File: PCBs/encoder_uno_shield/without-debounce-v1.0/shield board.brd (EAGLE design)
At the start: 71.7 x 53.5 mm, 9 parts, among them U1 ARDUINOR3-BPLACE

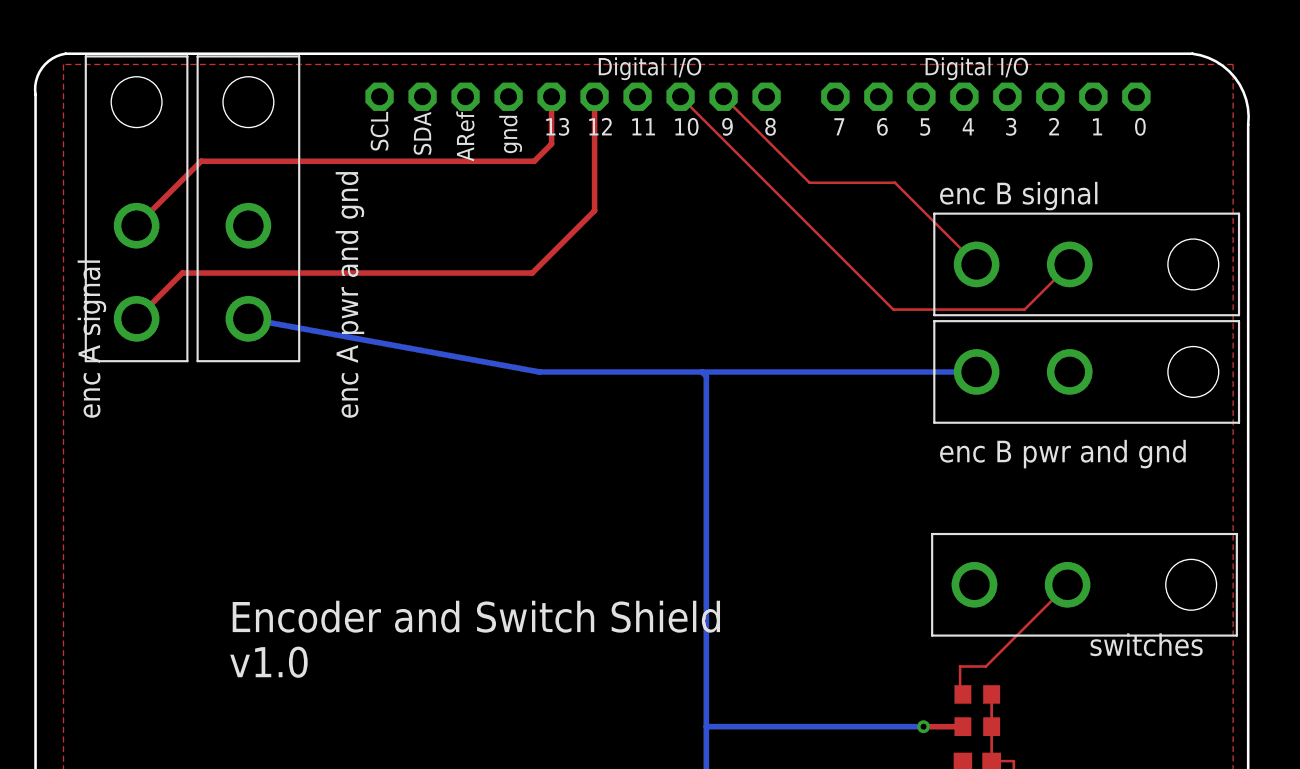
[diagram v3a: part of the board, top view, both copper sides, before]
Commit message: moved molex connectors further out to the edge
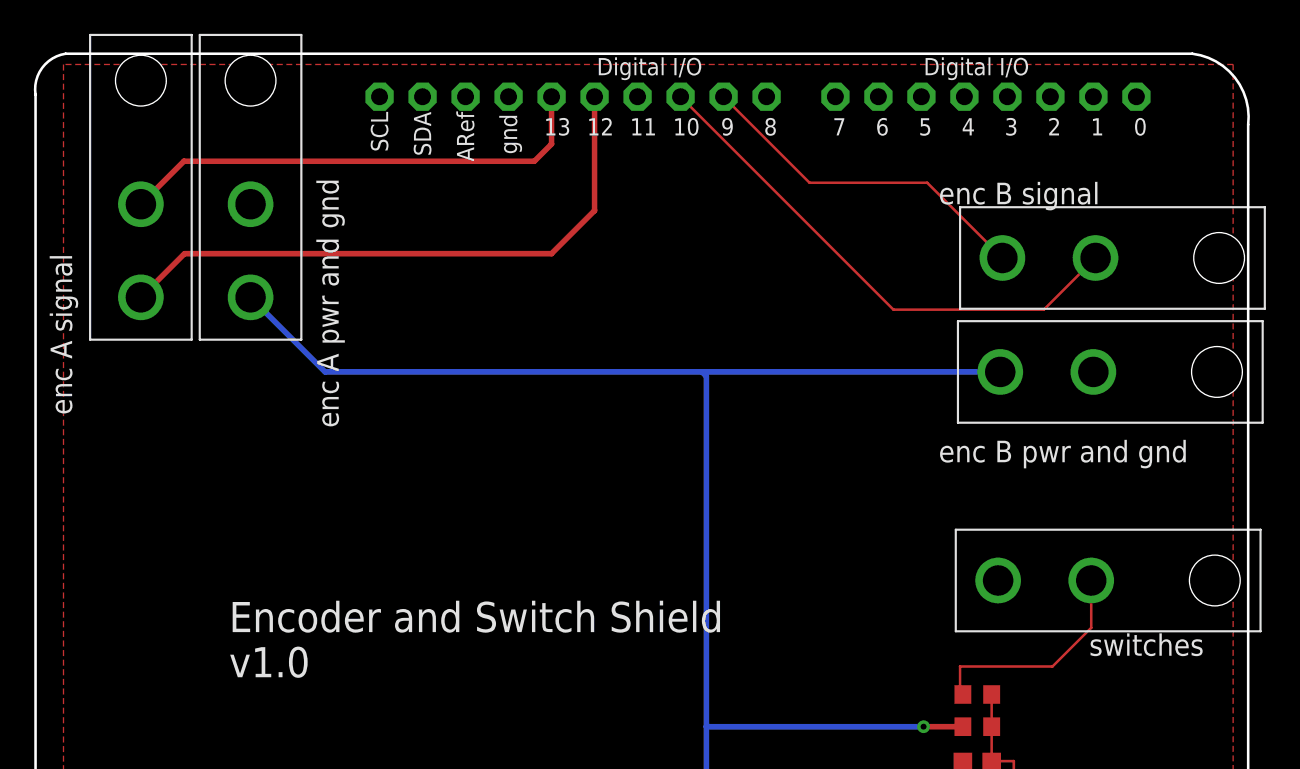
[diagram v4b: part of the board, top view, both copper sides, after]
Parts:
- moved U$6 1.57 mm to (103.3, 40.0)
- moved U$2 1.42 mm to (103.0, 21.0)
- moved U$3 1.40 mm to (103.1, 33.3)
- moved U$5 1.30 mm to (46.9, 43.2)
- moved U$4 1.28 mm to (53.3, 43.2)
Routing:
- net N$4: track 10.1 -> 13.2 mm
- net VCC: track 90.6 -> 93.4 mm
- net E2CHB: track 29.3 -> 31.0 mm
- net E2CHA: track 19.1 -> 20.4 mm
- net E1CHA: track 36.8 -> 36.0 mm
- net E1CHB: track 29.3 -> 28.5 mm
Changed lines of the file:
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@@
 <wire x1="112.268" y1="-0.635" x2="111.506" y2="-1.397" width="0.1524" layer="20" curve="-90"/>
 <wire x1="111.506" y1="-1.397" x2="42.164" y2="-1.397" width="0.1524" layer="20"/>
-<text x="59.69" y="30.48" size="1.27" layer="21" rot="R90">enc A pwr and gnd</text>
-<text x="44.45" y="30.48" size="1.27" layer="21" rot="R90">enc A signal</text>
+<text x="58.547" y="29.972" size="1.27" layer="21" rot="R90">enc A pwr and gnd</text>
+<text x="42.799" y="30.734" size="1.27" layer="21" rot="R90">enc A signal</text>
 <text x="93.98" y="27.94" size="1.27" layer="21">enc B pwr and gnd</text>
 <text x="93.98" y="43.18" size="1.27" layer="21">enc B signal</text>
@@
 <attribute name="VALUE" x="89.281" y="11.43" size="1.27" layer="26" rot="R180"/>
 </element>
-<element name="U$2" library="pat" package="MINI-FIT_JR_CONN" value="MOLEX_0039301022" x="101.6" y="20.701" smashed="yes" rot="R90"/>
-<element name="U$3" library="pat" package="MINI-FIT_JR_CONN" value="MOLEX_0039301022" x="101.727" y="33.274" smashed="yes" rot="R90"/>
-<element name="U$4" library="pat" package="MINI-FIT_JR_CONN" value="MOLEX_0039301022" x="53.213" y="41.91" smashed="yes" rot="R180"/>
-<element name="U$5" library="pat" package="MINI-FIT_JR_CONN" value="MOLEX_0039301022" x="46.609" y="41.91" smashed="yes" rot="R180"/>
-<element name="U$6" library="pat" package="MINI-FIT_JR_CONN" value="MOLEX_0039301022" x="101.727" y="39.624" smashed="yes" rot="R90"/>
+<element name="U$2" library="pat" package="MINI-FIT_JR_CONN" value="MOLEX_0039301022" x="102.997" y="20.955" smashed="yes" rot="R90"/>
+<element name="U$3" library="pat" package="MINI-FIT_JR_CONN" value="MOLEX_0039301022" x="103.124" y="33.274" smashed="yes" rot="R90"/>
+<element name="U$4" library="pat" package="MINI-FIT_JR_CONN" value="MOLEX_0039301022" x="53.34" y="43.18" smashed="yes" rot="R180"/>
+<element name="U$5" library="pat" package="MINI-FIT_JR_CONN" value="MOLEX_0039301022" x="46.863" y="43.18" smashed="yes" rot="R180"/>
+<element name="U$6" library="pat" package="MINI-FIT_JR_CONN" value="MOLEX_0039301022" x="103.251" y="40.005" smashed="yes" rot="R90"/>
 </elements>
 <signals>
@@
 <contactref element="U$3" pad="P$2"/>
 <contactref element="U$4" pad="P$2"/>
-<wire x1="70.391359375" y1="33.274" x2="53.213" y2="36.41" width="0.3302" layer="16"/>
-<wire x1="96.227" y1="33.274" x2="80.01" y2="33.274" width="0.3302" layer="16"/>
-<wire x1="80.01" y1="33.274" x2="70.391359375" y2="33.274" width="0.3302" layer="16"/>
+<wire x1="57.746" y1="33.274" x2="53.34" y2="37.68" width="0.3302" layer="16"/>
+<wire x1="97.624" y1="33.274" x2="80.01" y2="33.274" width="0.3302" layer="16"/>
+<wire x1="80.01" y1="33.274" x2="57.746" y2="33.274" width="0.3302" layer="16"/>
 <wire x1="80.264" y1="1.27" x2="80.264" y2="12.319" width="0.3302" layer="16"/>
 <wire x1="80.264" y1="12.319" x2="80.264" y2="33.02" width="0.3302" layer="16"/>
@@
 <contactref element="R3" pad="1"/>
 <contactref element="U$2" pad="P$1"/>
-<wire x1="101.6" y1="20.701" x2="96.774" y2="15.875" width="0.1524" layer="1"/>
-<wire x1="96.774" y1="15.875" x2="95.25" y2="15.875" width="0.1524" layer="1"/>
+<wire x1="102.997" y1="20.955" x2="102.997" y2="18.161" width="0.1524" layer="1"/>
+<wire x1="102.997" y1="18.161" x2="100.711" y2="15.875" width="0.1524" layer="1"/>
+<wire x1="100.711" y1="15.875" x2="95.25" y2="15.875" width="0.1524" layer="1"/>
 <wire x1="95.25" y1="15.875" x2="95.25" y2="14.39" width="0.1524" layer="1"/>
 <wire x1="95.25" y1="14.39" x2="95.416" y2="14.224" width="0.1524" layer="1"/>
@@
 <contactref element="U$5" pad="P$2"/>
 <wire x1="73.66" y1="49.149" x2="73.66" y2="49.53" width="0.1524" layer="1"/>
-<wire x1="46.609" y1="36.41" x2="49.315" y2="39.116" width="0.3302" layer="1"/>
+<wire x1="46.863" y1="37.68" x2="49.442" y2="40.259" width="0.3302" layer="1"/>
 <wire x1="73.66" y1="42.799" x2="73.66" y2="49.53" width="0.3302" layer="1"/>
-<wire x1="49.315" y1="39.116" x2="69.977" y2="39.116" width="0.3302" layer="1"/>
-<wire x1="69.977" y1="39.116" x2="73.66" y2="42.799" width="0.3302" layer="1"/>
+<wire x1="49.442" y1="40.259" x2="71.12" y2="40.259" width="0.3302" layer="1"/>
+<wire x1="71.12" y1="40.259" x2="73.66" y2="42.799" width="0.3302" layer="1"/>
 </signal>
 <signal name="E1CHB">
 <contactref element="U1" pad="D13"/>
 <contactref element="U$5" pad="P$1"/>
-<wire x1="46.609" y1="41.91" x2="50.419" y2="45.72" width="0.3302" layer="1"/>
-<wire x1="50.419" y1="45.72" x2="70.104" y2="45.72" width="0.3302" layer="1"/>
+<wire x1="46.863" y1="43.18" x2="49.403" y2="45.72" width="0.3302" layer="1"/>
+<wire x1="49.403" y1="45.72" x2="70.104" y2="45.72" width="0.3302" layer="1"/>
 <wire x1="70.104" y1="45.72" x2="71.12" y2="46.736" width="0.3302" layer="1"/>
 <wire x1="71.12" y1="46.736" x2="71.12" y2="49.53" width="0.3302" layer="1"/>
@@
 <contactref element="U1" pad="D10"/>
 <contactref element="U$6" pad="P$1"/>
-<wire x1="101.727" y1="39.624" x2="99.06" y2="36.957" width="0.1524" layer="1"/>
+<wire x1="103.251" y1="40.005" x2="100.203" y2="36.957" width="0.1524" layer="1"/>
 <wire x1="91.313" y1="36.957" x2="78.74" y2="49.53" width="0.1524" layer="1"/>
-<wire x1="99.06" y1="36.957" x2="91.313" y2="36.957" width="0.1524" layer="1"/>
+<wire x1="100.203" y1="36.957" x2="91.313" y2="36.957" width="0.1524" layer="1"/>
 </signal>
 <signal name="E2CHA">
 <contactref element="U1" pad="D9"/>
 <contactref element="U$6" pad="P$2"/>
-<wire x1="96.227" y1="39.624" x2="91.401" y2="44.45" width="0.1524" layer="1"/>
+<wire x1="97.751" y1="40.005" x2="93.306" y2="44.45" width="0.1524" layer="1"/>
 <wire x1="86.36" y1="44.45" x2="81.28" y2="49.53" width="0.1524" layer="1"/>
-<wire x1="91.401" y1="44.45" x2="86.36" y2="44.45" width="0.1524" layer="1"/>
+<wire x1="93.306" y1="44.45" x2="86.36" y2="44.45" width="0.1524" layer="1"/>
 </signal>
 </signals>

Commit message: added new version of encoder board
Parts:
- moved U$4 15.5 mm to (52.8, 58.7)
- moved U$5 15.5 mm to (46.4, 58.7)
- moved U$3 13.0 mm to (116.1, 33.9)
- moved U$2 13.0 mm to (116.0, 21.6)
- moved U$6 13.0 mm to (116.2, 40.6)
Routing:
- net VCC: track 93.4 -> 113.9 mm
- net N$4: track 13.2 -> 26.6 mm
- net E2CHB: track 31.0 -> 43.7 mm
- net E2CHA: track 20.4 -> 33.1 mm
- net E1CHA: track 36.0 -> 33.2 mm
- net E1CHB: track 28.5 -> 30.7 mm
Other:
- board size 71.7 x 53.5 mm -> 86.7 x 72.1 mm
- board text added: "Encoder and Switch Shield v1.1"
- board text removed: "Encoder and Switch Shield v1.0"
